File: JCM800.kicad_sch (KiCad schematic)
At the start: 113 parts, among them U1 ECC83, U2 ECC83, U3 ECC83, U4 EL84, U5 EL84

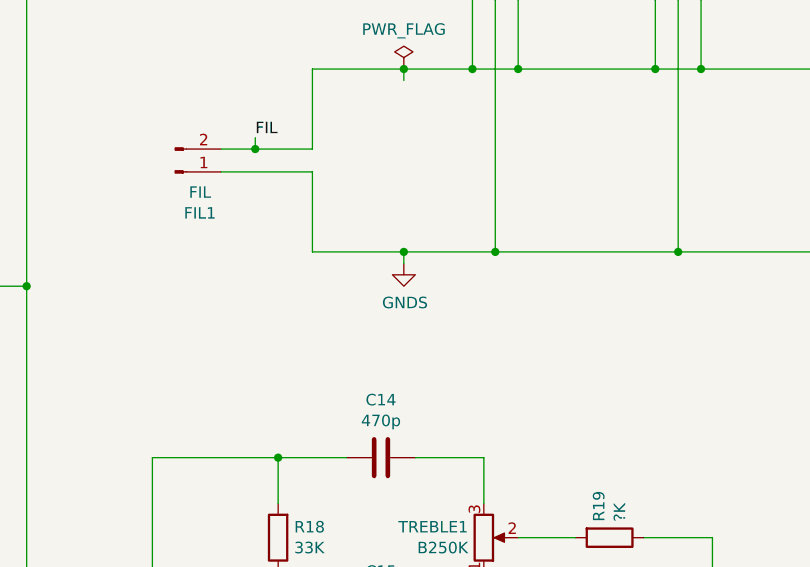
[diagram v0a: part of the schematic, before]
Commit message: Floating Filaments on pins 9 for triodes and 5 for pentodes
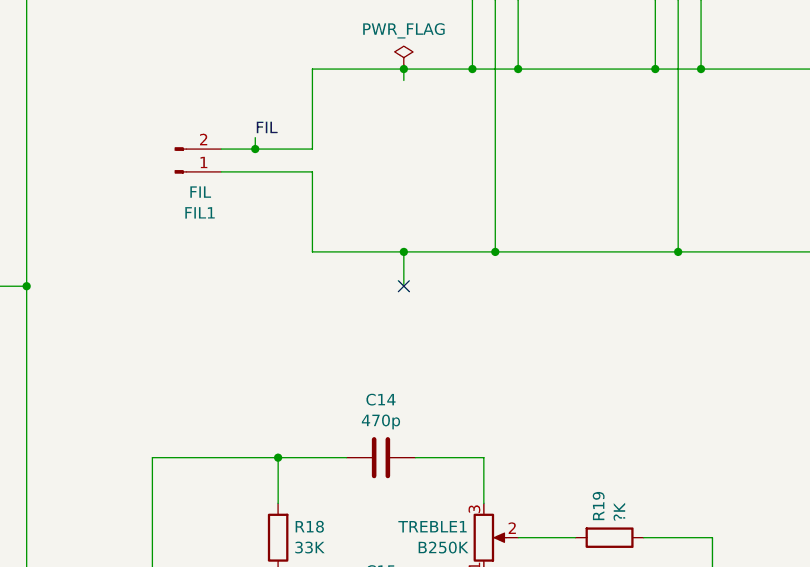
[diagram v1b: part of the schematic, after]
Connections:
- net GNDS: no longer FIL1.1 (Pin_1), U1.9 (F2), U2.9 (F2), U3.9 (F2), U4.5 (F2), U5.5 (F2)
- new net: FIL1.1 (Pin_1), U1.9 (F2), U2.9 (F2), U3.9 (F2), U4.5 (F2), U5.5 (F2)
- no-connect marks 5 -> 6
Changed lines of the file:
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@@
 	)
 	(junction
-		(at 341.63 73.66)
+		(at 265.43 73.66)
 		(diameter 0)
 		(color 0 0 0 0)
 	)
 	(junction
-		(at 265.43 73.66)
+		(at 341.63 73.66)
 		(diameter 0)
 		(color 0 0 0 0)
@@
 	)
 	(no_connect
+		(at 265.43 77.47)
+	)
+	(no_connect
 		(at 33.02 49.53)
 	)
@@
 	(wire
 		(pts
-			(xy 265.43 73.66) (xy 275.59 73.66)
+			(xy 255.27 73.66) (xy 265.43 73.66)
 		)
 		(stroke
@@
 	(wire
 		(pts
-			(xy 265.43 73.66) (xy 265.43 74.93)
-		)
-		(stroke
-			(width 0)
-			(type default)
-		)
-	)
-	(wire
-		(pts
 			(xy 274.32 109.22) (xy 274.32 115.57)
 		)
@@
 	(wire
 		(pts
+			(xy 265.43 73.66) (xy 265.43 77.47)
+		)
+		(stroke
+			(width 0)
+			(type default)
+		)
+	)
+	(wire
+		(pts
 			(xy 177.8 80.01) (xy 177.8 77.47)
 		)
@@
 	(wire
 		(pts
-			(xy 255.27 73.66) (xy 265.43 73.66)
-		)
-		(stroke
-			(width 0)
-			(type default)
-		)
-	)
-	(wire
-		(pts
 			(xy 196.85 77.47) (xy 196.85 76.2)
 		)
@@
 	(wire
 		(pts
+			(xy 265.43 73.66) (xy 275.59 73.66)
+		)
+		(stroke
+			(width 0)
+			(type default)
+		)
+	)
+	(wire
+		(pts
 			(xy 132.08 113.03) (xy 132.08 116.84)
 		)
@@
 					(unit 1)
 				)
-			)
-		)
-	)
-	(symbol
-		(lib_id "power:GNDS")
-		(at 265.43 74.93 0)
-		(unit 1)
-		(exclude_from_sim no)
-		(in_bom yes)
-		(on_board yes)
-		(dnp no)
-		(property "Reference" "#PWR0101"
-			(at 265.43 81.28 0)
-			(effects
-				(font
-					(size 1.27 1.27)
-				)
-				(hide yes)
-			)
-		)
-		(property "Value" "GNDS"
-			(at 265.557 79.3242 0)
-			(effects
-				(font
-					(size 1.27 1.27)
-				)
-			)
-		)
-		(property "Footprint" ""
-			(at 265.43 74.93 0)
-			(effects
-				(font
-					(size 1.27 1.27)
-				)
-				(hide yes)
-			)
-		)
-		(property "Datasheet" ""
-			(at 265.43 74.93 0)
-			(effects
-				(font
-					(size 1.27 1.27)
-				)
-				(hide yes)
-			)
-		)
-		(property "Description" ""
-			(at 265.43 74.93 0)
-			(effects
-				(font
-					(size 1.27 1.27)
-				)
-			)
-		)
-		(pin "1"
-		)
-		(instances
-			(project ""
-				(path "/b5953cb0-a383-4f71-9a8d-0d018e66526c"
-					(reference "#PWR0101")
-					(unit 1)
-				)
